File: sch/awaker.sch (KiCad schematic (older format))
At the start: 35 parts, among them P1 CONN_01X03, P2 CONN_01X07, P3 uart, P4 swd, P5 CONN_01X06, P6 speaker, P7 pow_led, P8 power, P9 CONN_01X07, Q1 Q_NMOS_GDS, SW1 SW_PUSH, U1 STM32F100C4, U2 AP1117D33, Y1 8Mhz, Y2 32768

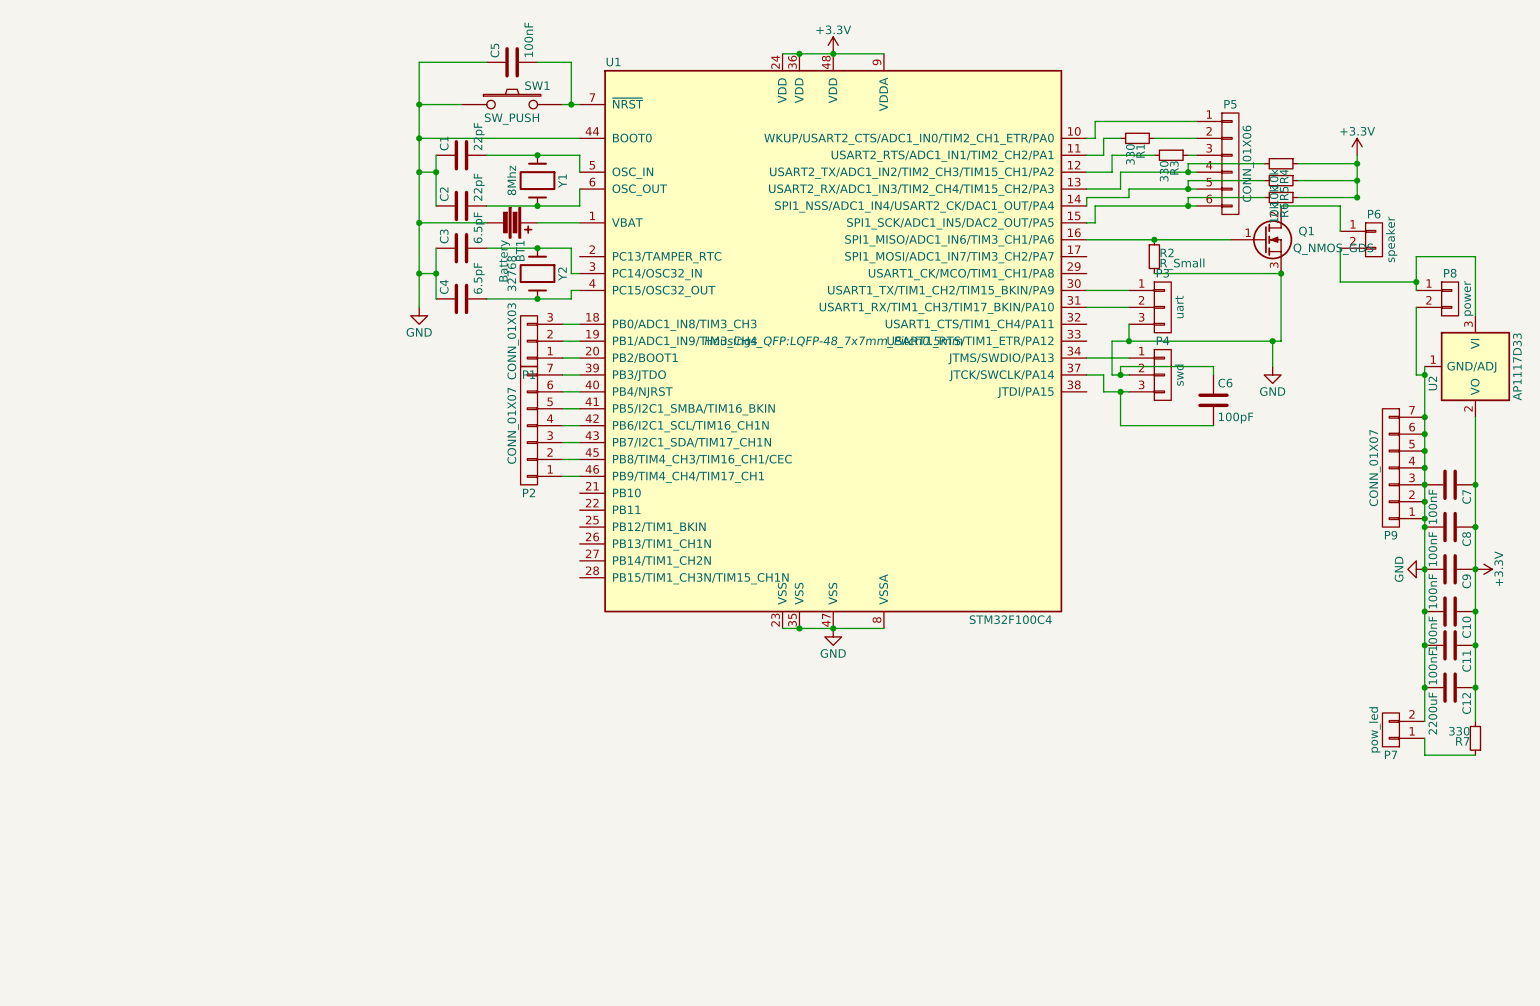
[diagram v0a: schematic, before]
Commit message: reset. New board.
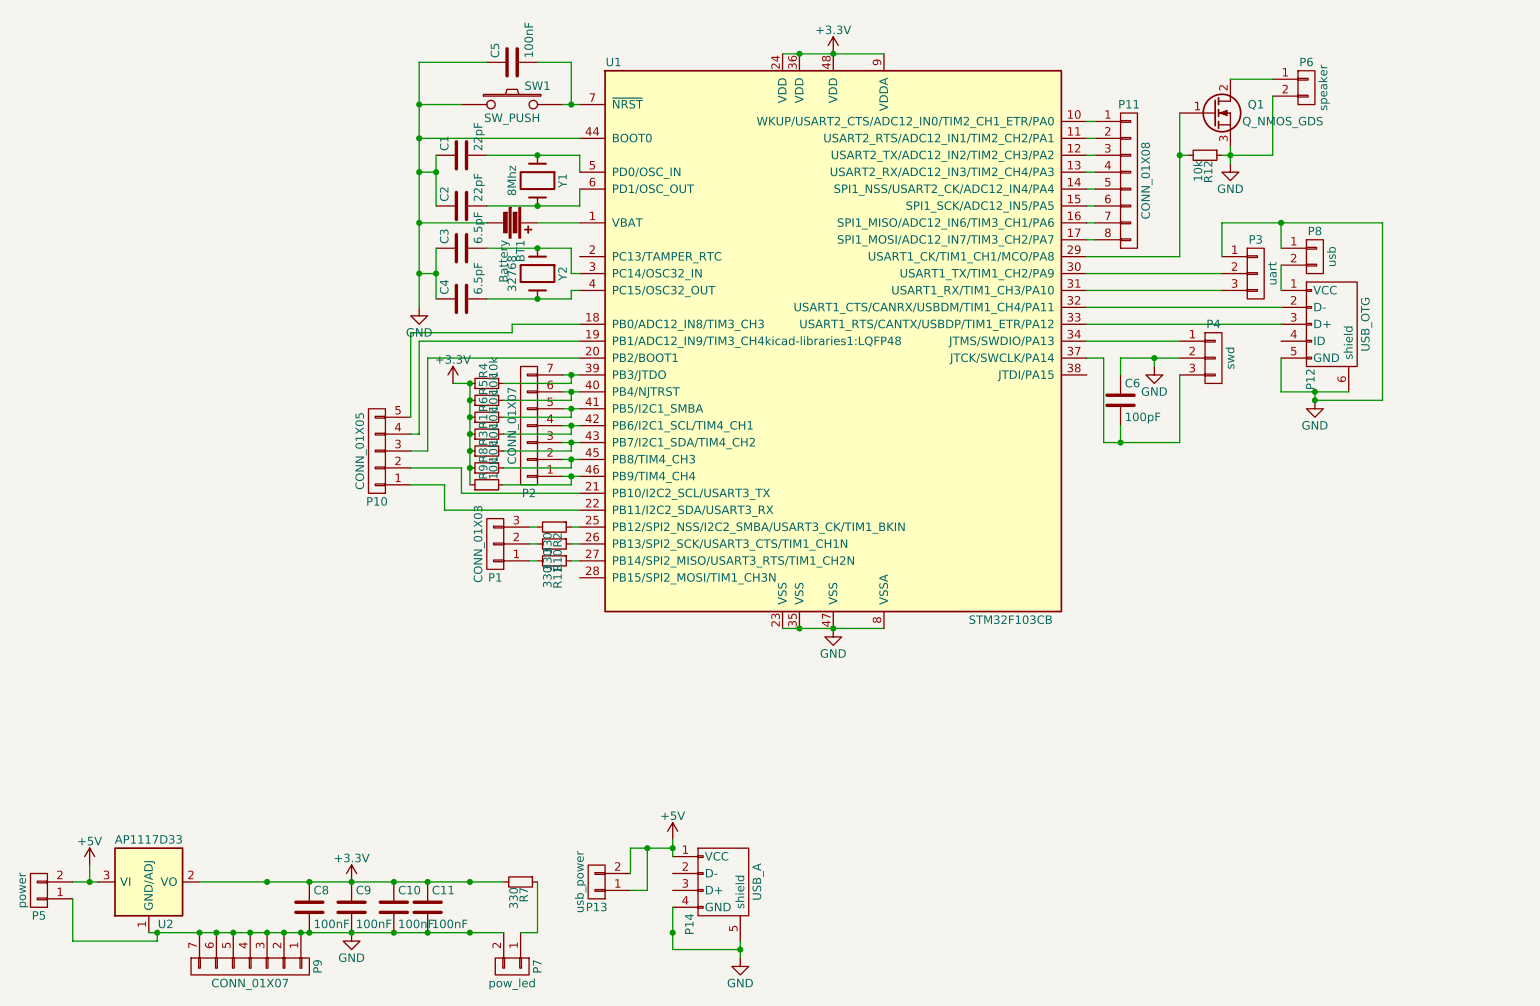
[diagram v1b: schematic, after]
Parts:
- removed C12: 2200uF, Capacitors_ThroughHole:C_Radial_D8_L11.5_P3.5, symbol C
- removed C7: 100nF, Capacitors_SMD:C_0402, symbol C
- removed P5: CONN_01X06, Pin_Headers:Pin_Header_Straight_1x06, symbol CONN_01X06
- removed U1: STM32F100C4, Housings_QFP:LQFP-48_7x7mm_Pitch0.5mm, symbol STM32F100C4
- added P10: CONN_01X05, Pin_Headers:Pin_Header_Straight_1x05, symbol CONN_01X05
- added P11: CONN_01X08, Pin_Headers:Pin_Header_Straight_1x08, symbol CONN_01X08
- added P12: USB_OTG, kicad-libraries1:USB-MINI-B-SMD, symbol USB_OTG
- added P13: usb_power, Pin_Headers:Pin_Header_Straight_1x02, symbol CONN_01X02
- added P14: USB_A, kicad-libraries1:USB-A-SMT-8231-PEG, symbol USB_A
- added P5: power, Pin_Headers:Pin_Header_Straight_1x02, symbol CONN_01X02
- added R10, R11: 330, Resistors_SMD:R_0603, symbol R_Small
- added R12, R8, R9: 10k, Resistors_SMD:R_0603, symbol R_Small
- added U1: STM32F103CB, kicad-libraries1:LQFP48, symbol STM32F103CB
- P8: value power -> usb
- R1, R3: value 330 -> 10k
- R2: value R_Small -> 330
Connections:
- net +3V3: now also R1.1, R3.1, R8.1, R9.1, U1.24 (VDD), U1.36 (VDD), U1.48 (VDD), U1.9 (VDDA)
- net GND: now also P3.1 (P1), P6.2 (P2), P8.1 (P1), P12.5 (GND), P12.6 (shield), P14.4 (GND), P14.5 (shield), P5.1 (P1), R12.1, U1.23 (VSS), U1.35 (VSS), U1.44 (BOOT0), U1.47 (VSS), U1.8 (VSSA); no longer P3.3 (P3), P8.2 (P2), R2.2
- net at BT1.1: now also U1.1 (VBAT)
- net at R1.2: now also P2.4 (P4), U1.42 (PB6/I2C1_SCL/TIM4_CH1)
- net at R3.2: now also P2.3 (P3), U1.43 (PB7/I2C1_SDA/TIM4_CH2)
- net at R4.2: now also P2.7 (P7), U1.39 (PB3/JTDO)
- net at R5.2: now also P2.6 (P6), U1.40 (PB4/NJTRST)
- net at R6.2: now also P2.5 (P5), U1.41 (PB5/I2C1_SMBA)
- net at Q1.1 (G): now also R12.2, U1.29 (USART1_CK/TIM1_CH1/MCO/PA8); no longer R2.1
- net at P1.3 (P3): now also R2.2
- net at P1.2 (P2): now also R10.2
- net at P1.1 (P1): now also R11.2
- net at C3.2, Y2.1: now also U1.3 (PC14/OSC32_IN)
- net at P3.2 (P2): now also U1.30 (USART1_TX/TIM1_CH2/PA9)
- net at P4.1 (P1): now also U1.34 (JTMS/SWDIO/PA13)
- net at C6.2, P4.3 (P3): now also U1.37 (JTCK/SWCLK/PA14)
- net at C4.2, Y2.2: now also U1.4 (PC15/OSC32_OUT)
- net at P2.2 (P2): now also R8.2, U1.45 (PB8/TIM4_CH3)
- net at P2.1 (P1): now also R9.2, U1.46 (PB9/TIM4_CH4)
- net at C1.2, Y1.1: now also U1.5 (PD0/OSC_IN)
- net at C2.2, Y1.2: now also U1.6 (PD1/OSC_OUT)
- net at C5.2, SW1.2: now also U1.7 (~NRST)
- new net: R2.1, U1.25 (PB12/SPI2_NSS/I2C2_SMBA/USART3_CK/TIM1_BKIN)
- new net: P3.3 (P3), U1.31 (USART1_RX/TIM1_CH3/PA10)
- new net: P12.1 (VCC), P8.2 (P2)
- new net: P11.1 (P1), U1.10 (WKUP/USART2_CTS/ADC12_IN0/TIM2_CH1_ETR/PA0)
- new net: P11.2 (P2), U1.11 (USART2_RTS/ADC12_IN1/TIM2_CH2/PA1)
- new net: P11.3 (P3), U1.12 (USART2_TX/ADC12_IN2/TIM2_CH3/PA2)
- new net: P11.4 (P4), U1.13 (USART2_RX/ADC12_IN3/TIM2_CH4/PA3)
- new net: P11.5 (P5), U1.14 (SPI1_NSS/USART2_CK/ADC12_IN4/PA4)
- new net: P11.6 (P6), U1.15 (SPI1_SCK/ADC12_IN5/PA5)
- new net: P11.7 (P7), U1.16 (SPI1_MISO/ADC12_IN6/TIM3_CH1/PA6)
- new net: P11.8 (P8), U1.17 (SPI1_MOSI/ADC12_IN7/TIM3_CH2/PA7)
- new net: P10.5 (P5), U1.18 (PB0/ADC12_IN8/TIM3_CH3)
- new net: P10.4 (P4), U1.19 (PB1/ADC12_IN9/TIM3_CH4)
- new net: P10.3 (P3), U1.20 (PB2/BOOT1)
- new net: P10.2 (P2), U1.21 (PB10/I2C2_SCL/USART3_TX)
- new net: P10.1 (P1), U1.22 (PB11/I2C2_SDA/USART3_RX)
- new net: R10.1, U1.26 (PB13/SPI2_SCK/USART3_CTS/TIM1_CH1N)
- new net: R11.1, U1.27 (PB14/SPI2_MISO/USART3_RTS/TIM1_CH2N)
- new net: P12.2 (D-), U1.32 (USART1_CTS/CANRX/USBDM/TIM1_CH4/PA11)
- new net: P12.3 (D+), U1.33 (USART1_RTS/CANTX/USBDP/TIM1_ETR/PA12)
- new net +5V: P13.1 (P1), P13.2 (P2), P14.1 (VCC), P5.2 (P2), U2.3 (VI)
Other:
- moved on the sheet: C10, C11, C6, C8, C9, P1, P3, P4, P6, P7, P8, P9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
